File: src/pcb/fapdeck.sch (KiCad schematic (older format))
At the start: 0 parts

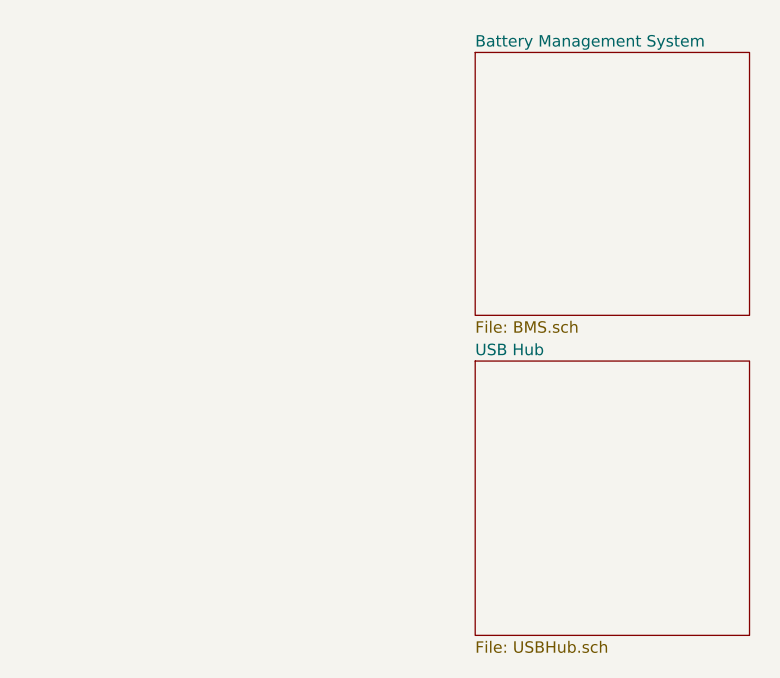
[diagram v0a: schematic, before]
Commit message: added hierarchy for mcu and usb selector
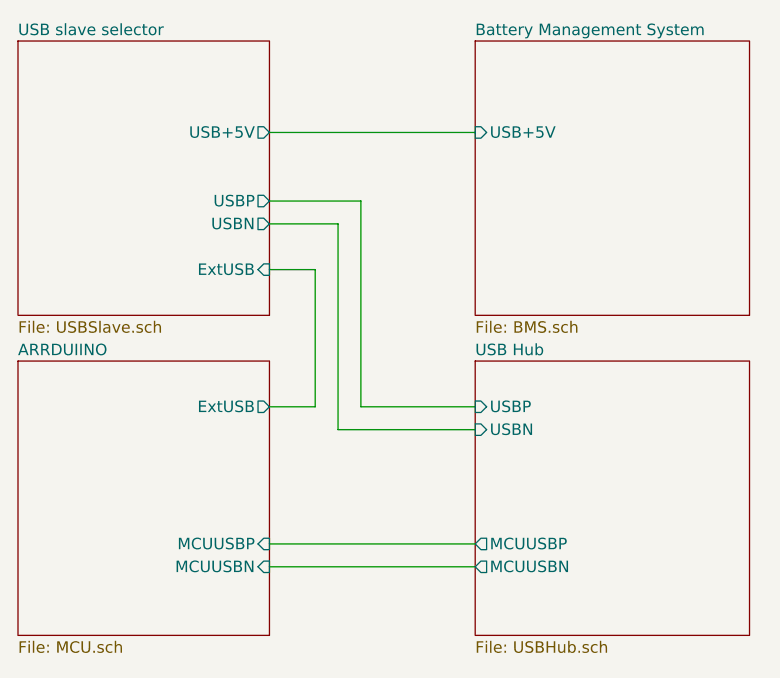
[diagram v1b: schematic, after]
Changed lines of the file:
@@
 EESchema Schematic File Version 4
+LIBS:fapdeck-cache
 EELAYER 26 0
 EELAYER END
 $Descr A4 11693 8268
 encoding utf-8
-Sheet 1 3
+Sheet 1 5
 Title ""
 Date ""
@@
 $EndDescr
 $Sheet
-S 6300 2050 1200 1150
+S 6300 2000 1200 1200
 U 5C03C416
 F0 "Battery Management System" 50
 F1 "BMS.sch" 50
+F2 "USB+5V" I L 6300 2400 50
 $EndSheet
 $Sheet
@@
 F0 "USB Hub" 50
 F1 "USBHub.sch" 50
+F2 "USBP" I L 6300 3600 50
+F3 "USBN" I L 6300 3700 50
+F4 "MCUUSBP" O L 6300 4200 50
+F5 "MCUUSBN" O L 6300 4300 50
 $EndSheet
+$Sheet
+S 4300 2000 1100 1200
+U 5C1FAD08
+F0 "USB slave selector" 50
+F1 "USBSlave.sch" 50
+F2 "ExtUSB" I R 5400 3000 50
+F3 "USBP" O R 5400 2700 50
+F4 "USBN" O R 5400 2800 50
+F5 "USB+5V" O R 5400 2400 50
+$EndSheet
+$Sheet
+S 4300 3400 1100 1200
+U 5C1FAF8C
+F0 "ARRDUIINO" 50
+F1 "MCU.sch" 50
+F2 "MCUUSBP" I R 5400 4200 50
+F4 "ExtUSB" O R 5400 3600 50
+F5 "MCUUSBN" I R 5400 4300 50
+$EndSheet
+Wire Wire Line
+	5700 3700 6300 3700
+Wire Wire Line
+	6300 3600 5800 3600
+Wire Wire Line
+	6300 4200 5400 4200
+Wire Wire Line
+	5400 4300 6300 4300
+Wire Wire Line
+	5400 2400 6300 2400
+Wire Wire Line
+	5400 2700 5800 2700
+Wire Wire Line
+	5700 2800 5400 2800
+Wire Wire Line
+	5800 2700 5800 3600
+Wire Wire Line
+	5700 2800 5700 3700
+Wire Wire Line
+	5400 3000 5600 3000
+Wire Wire Line
+	5600 3000 5600 3600
+Wire Wire Line
+	5600 3600 5400 3600
 $EndSCHEMATC

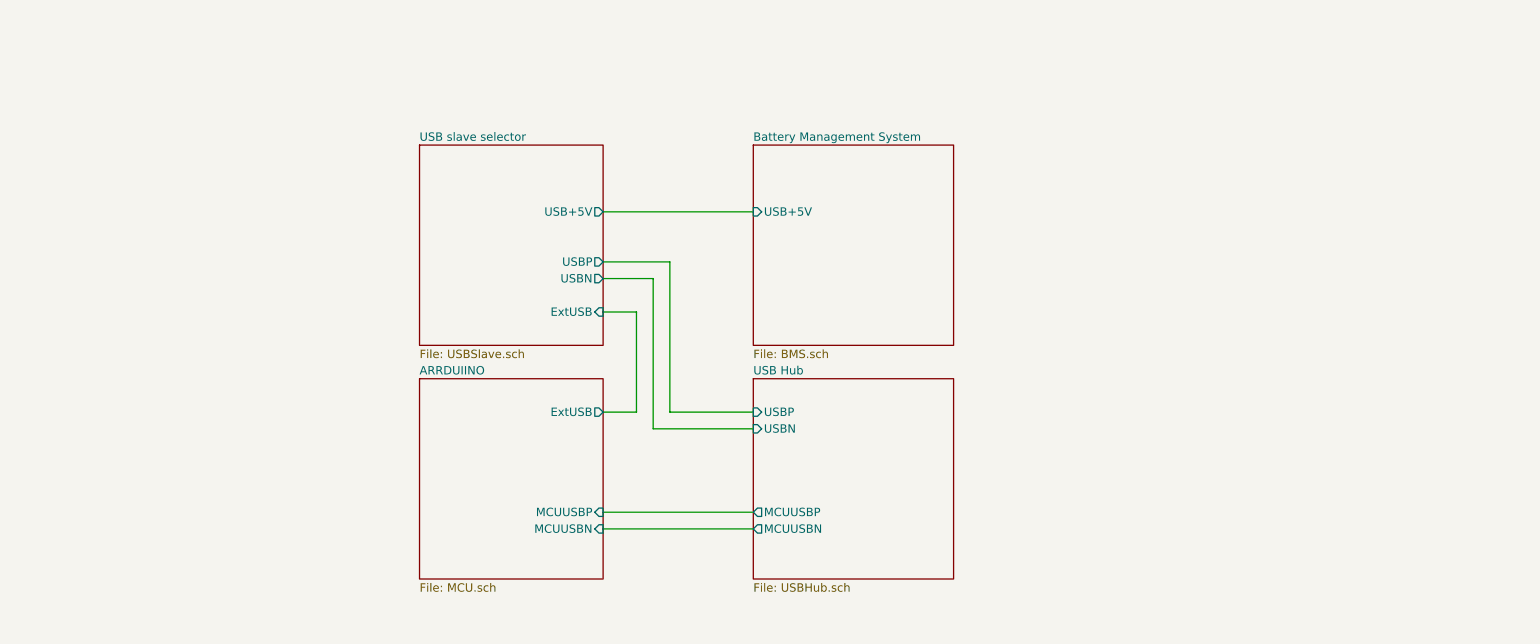
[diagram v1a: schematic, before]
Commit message: added more connections, clarified schematic. Also added missing schematics
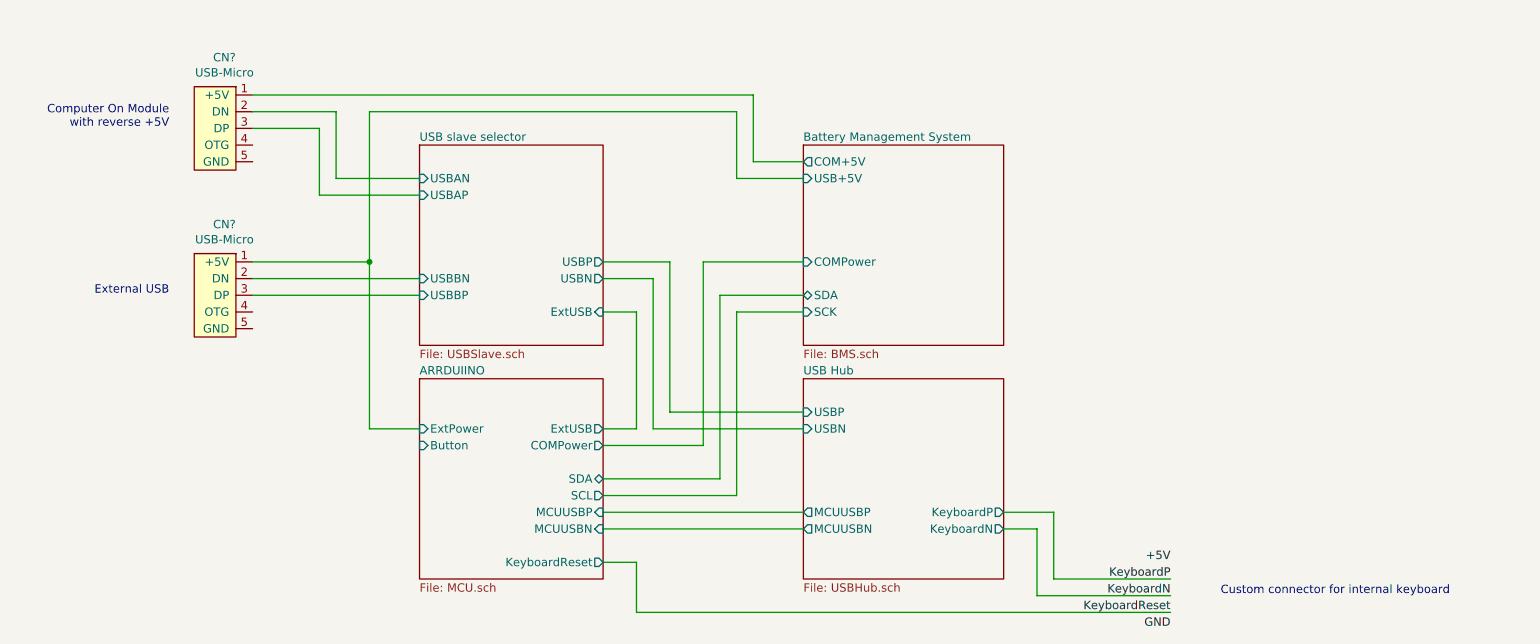
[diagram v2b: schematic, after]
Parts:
- added CN? (x2): USB-Micro, symbol Generic:USB-Micro
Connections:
- new net ARRDUIINO/ExtPower: CN?.1 (+5V)
- new net Battery Management System/COM+5V: CN?.1 (+5V)
- new net USB slave selector/USBAN: CN?.2 (DN)
- new net USB slave selector/USBAP: CN?.3 (DP)
- new net USB slave selector/USBBN: CN?.2 (DN)
- new net USB slave selector/USBBP: CN?.3 (DP)
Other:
- note added: "Computer On Module\nwith reverse +5V"
- note added: "Custom connector for internal keyboard"
- note added: "External USB"
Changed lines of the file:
@@
 $EndDescr
 $Sheet
-S 6300 2000 1200 1200
+S 6600 2000 1200 1200
 U 5C03C416
 F0 "Battery Management System" 50
 F1 "BMS.sch" 50
-F2 "USB+5V" I L 6300 2400 50
+F2 "USB+5V" I L 6600 2200 50
+F3 "COM+5V" O L 6600 2100 50
+F4 "COMPower" I L 6600 2700 50
+F5 "SDA" B L 6600 2900 50
+F6 "SCK" I L 6600 3000 50
 $EndSheet
 $Sheet
-S 6300 3400 1200 1200
+S 6600 3400 1200 1200
 U 5C03C43A
 F0 "USB Hub" 50
 F1 "USBHub.sch" 50
-F2 "USBP" I L 6300 3600 50
-F3 "USBN" I L 6300 3700 50
-F4 "MCUUSBP" O L 6300 4200 50
-F5 "MCUUSBN" O L 6300 4300 50
+F2 "USBP" I L 6600 3600 50
+F3 "USBN" I L 6600 3700 50
+F4 "MCUUSBP" O L 6600 4200 50
+F5 "MCUUSBN" O L 6600 4300 50
+F6 "KeyboardP" O R 7800 4200 50
+F7 "KeyboardN" O R 7800 4300 50
 $EndSheet
 $Sheet
@@
 F3 "USBP" O R 5400 2700 50
 F4 "USBN" O R 5400 2800 50
-F5 "USB+5V" O R 5400 2400 50
+F5 "USBAN" I L 4300 2200 50
+F6 "USBAP" I L 4300 2300 50
+F7 "USBBN" I L 4300 2800 50
+F8 "USBBP" I L 4300 2900 50
 $EndSheet
 $Sheet
@@
 F1 "MCU.sch" 50
 F2 "MCUUSBP" I R 5400 4200 50
-F4 "ExtUSB" O R 5400 3600 50
-F5 "MCUUSBN" I R 5400 4300 50
+F3 "ExtUSB" O R 5400 3700 50
+F4 "MCUUSBN" I R 5400 4300 50
+F5 "KeyboardReset" O R 5400 4500 50
+F6 "COMPower" O R 5400 3800 50
+F7 "SDA" B R 5400 4000 50
+F8 "SCL" O R 5400 4100 50
+F9 "Button" I L 4300 3800 50
+F10 "ExtPower" I L 4300 3700 50
 $EndSheet
 Wire Wire Line
-	5700 3700 6300 3700
+	5700 3700 6600 3700
 Wire Wire Line
-	6300 3600 5800 3600
+	6600 3600 5800 3600
 Wire Wire Line
-	6300 4200 5400 4200
+	6600 4200 5400 4200
 Wire Wire Line
-	5400 4300 6300 4300
-Wire Wire Line
-	5400 2400 6300 2400
+	5400 4300 6600 4300
 Wire Wire Line
 	5400 2700 5800 2700
@@
 	5400 3000 5600 3000
 Wire Wire Line
-	5600 3000 5600 3600
+	5600 3000 5600 3700
 Wire Wire Line
-	5600 3600 5400 3600
+	5600 3700 5400 3700
+Wire Wire Line
+	5400 4500 5600 4500
+Wire Wire Line
+	5600 4500 5600 4800
+Wire Wire Line
+	5600 4800 8800 4800
+Wire Wire Line
+	7800 4300 8000 4300
+Wire Wire Line
+	8000 4300 8000 4700
+Wire Wire Line
+	8000 4700 8800 4700
+Wire Wire Line
+	7800 4200 8100 4200
+Wire Wire Line
+	8100 4200 8100 4600
+Wire Wire Line
+	8100 4600 8800 4600
+Text Label 8800 4500 2    50   ~ 0
++5V
+Text Label 8800 4600 2    50   ~ 0
+KeyboardP
+Text Label 8800 4700 2    50   ~ 0
+KeyboardN
+Text Label 8800 4800 2    50   ~ 0
+KeyboardReset
+Text Label 8800 4900 2    50   ~ 0
+GND
+Wire Wire Line
+	5400 3800 6000 3800
+Wire Wire Line
+	6000 3800 6000 2700
+Wire Wire Line
+	6000 2700 6600 2700
+Wire Wire Line
+	6600 2900 6100 2900
+Wire Wire Line
+	6100 2900 6100 4000
+Wire Wire Line
+	6100 4000 5400 4000
+Wire Wire Line
+	5400 4100 6200 4100
+Wire Wire Line
+	6200 4100 6200 3000
+Wire Wire Line
+	6200 3000 6600 3000
+$Comp
+L Generic:USB-Micro CN?
+U 1 1 5C292499
+P 3200 1800
+AR Path="/5C1FAD08/5C292499" Ref="CN?"  Part="1"
+AR Path="/5C292499" Ref="CN?"  Part="1"
+F 0 "CN?" H 3269 2125 50  0000 C CNN
+F 1 "USB-Micro" H 3269 2034 50  0000 C CNN
+F 2 "" H 3200 1800 50  0001 C CNN
+F 3 "" H 3200 1800 50  0001 C CNN
+	1    3200 1800
+	-1   0    0    -1
+$EndComp
+$Comp
+L Generic:USB-Micro CN?
+U 1 1 5C2924A0
+P 3200 2800
+AR Path="/5C1FAD08/5C2924A0" Ref="CN?"  Part="1"
+AR Path="/5C2924A0" Ref="CN?"  Part="1"
+F 0 "CN?" H 3269 3125 50  0000 C CNN
+F 1 "USB-Micro" H 3269 3034 50  0000 C CNN
+F 2 "" H 3200 2800 50  0001 C CNN
+F 3 "" H 3200 2800 50  0001 C CNN
+	1    3200 2800
+	-1   0    0    -1
+$EndComp
+Wire Wire Line
+	6600 2100 6300 2100
+Wire Wire Line
+	6300 2100 6300 1700
+Wire Wire Line
+	6300 1700 3300 1700
+Wire Wire Line
+	4300 2800 3300 2800
+Wire Wire Line
+	3300 2900 4300 2900
+Wire Wire Line
+	3300 1800 3800 1800
+Wire Wire Line
+	3800 1800 3800 2200
+Wire Wire Line
+	3800 2200 4300 2200
+Wire Wire Line
+	4300 2300 3700 2300
+Wire Wire Line
+	3700 2300 3700 1900
+Wire Wire Line
+	3700 1900 3300 1900
+Wire Wire Line
+	3300 2700 4000 2700
+Wire Wire Line
+	4000 2700 4000 1800
+Wire Wire Line
+	4000 1800 6200 1800
+Wire Wire Line
+	6200 1800 6200 2200
+Wire Wire Line
+	6200 2200 6600 2200
+Text Notes 2800 1900 2    50   ~ 0
+Computer On Module\nwith reverse +5V
+Text Notes 2800 2900 2    50   ~ 0
+External USB
+Text Notes 9100 4700 0    50   ~ 0
+Custom connector for internal keyboard
+Wire Wire Line
+	4300 3700 4000 3700
+Wire Wire Line
+	4000 3700 4000 2700
+Connection ~ 4000 2700
 $EndSCHEMATC

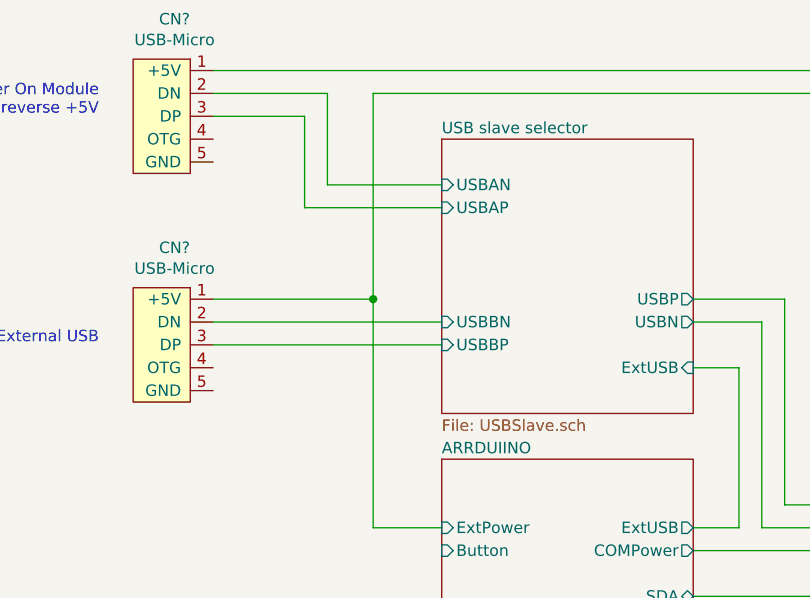
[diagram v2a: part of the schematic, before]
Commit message: added usb demux
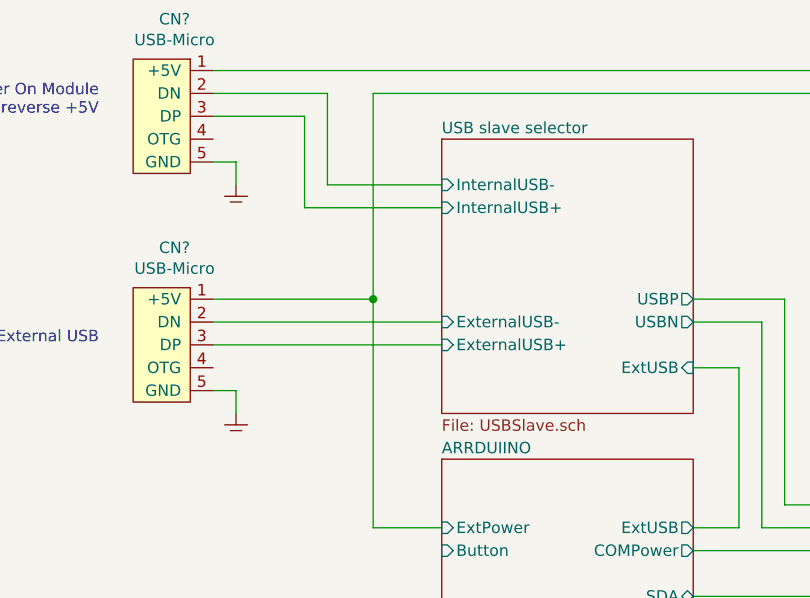
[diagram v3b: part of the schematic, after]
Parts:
- added GND? (x2): GND, symbol Generic:GND
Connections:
- net at CN?.5 (GND): now also GND?.1 (GND) (x2)
- net USB slave selector/USBAN renamed USB slave selector/InternalUSB-
- net USB slave selector/USBAP renamed USB slave selector/InternalUSB+
- net USB slave selector/USBBN renamed USB slave selector/ExternalUSB-
- net USB slave selector/USBBP renamed USB slave selector/ExternalUSB+
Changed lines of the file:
@@
 F3 "USBP" O R 5400 2700 50
 F4 "USBN" O R 5400 2800 50
-F5 "USBAN" I L 4300 2200 50
-F6 "USBAP" I L 4300 2300 50
-F7 "USBBN" I L 4300 2800 50
-F8 "USBBP" I L 4300 2900 50
+F5 "InternalUSB-" I L 4300 2200 50
+F6 "InternalUSB+" I L 4300 2300 50
+F7 "ExternalUSB-" I L 4300 2800 50
+F8 "ExternalUSB+" I L 4300 2900 50
 $EndSheet
 $Sheet
@@
 	4000 3700 4000 2700
 Connection ~ 4000 2700
+$Comp
+L Generic:GND GND?
+U 1 1 5CA87BF8
+P 3400 2200
+F 0 "GND?" H 3550 2250 50  0001 C CNN
+F 1 "GND" H 3550 2200 50  0001 C CNN
+F 2 "" H 3400 2200 50  0001 C CNN
+F 3 "" H 3400 2200 50  0001 C CNN
+	1    3400 2200
+	1    0    0    -1
+$EndComp
+Wire Wire Line
+	3300 2100 3400 2100
+Wire Wire Line
+	3400 2100 3400 2200
+$Comp
+L Generic:GND GND?
+U 1 1 5CA888D8
+P 3400 3200
+F 0 "GND?" H 3550 3250 50  0001 C CNN
+F 1 "GND" H 3550 3200 50  0001 C CNN
+F 2 "" H 3400 3200 50  0001 C CNN
+F 3 "" H 3400 3200 50  0001 C CNN
+	1    3400 3200
+	1    0    0    -1
+$EndComp
+Wire Wire Line
+	3300 3100 3400 3100
+Wire Wire Line
+	3400 3100 3400 3200
 $EndSCHEMATC

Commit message: tweaked libraries
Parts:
- CN? (x2): symbol Generic:USB-Micro -> generic:USB-Micro
- GND? (x2): symbol Generic:GND -> generic:GND
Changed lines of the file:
@@
 	6200 3000 6600 3000
 $Comp
-L Generic:USB-Micro CN?
+L generic:USB-Micro CN?
 U 1 1 5C292499
 P 3200 1800
@@
 $EndComp
 $Comp
-L Generic:USB-Micro CN?
+L generic:USB-Micro CN?
 U 1 1 5C2924A0
 P 3200 2800
@@
 Connection ~ 4000 2700
 $Comp
-L Generic:GND GND?
+L generic:GND GND?
 U 1 1 5CA87BF8
 P 3400 2200
@@
 	3400 2100 3400 2200
 $Comp
-L Generic:GND GND?
+L generic:GND GND?
 U 1 1 5CA888D8
 P 3400 3200
